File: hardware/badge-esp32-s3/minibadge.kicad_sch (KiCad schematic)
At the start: 10 parts, among them J10 Conn_01x02_Socket, J3 Conn_01x02_Socket, J4 Conn_01x02_Socket, J5 Conn_01x02_Socket, J6 Conn_01x04_Socket, J7 Conn_01x02_Socket, J8 Conn_01x04_Socket, J9 Conn_01x02_Socket

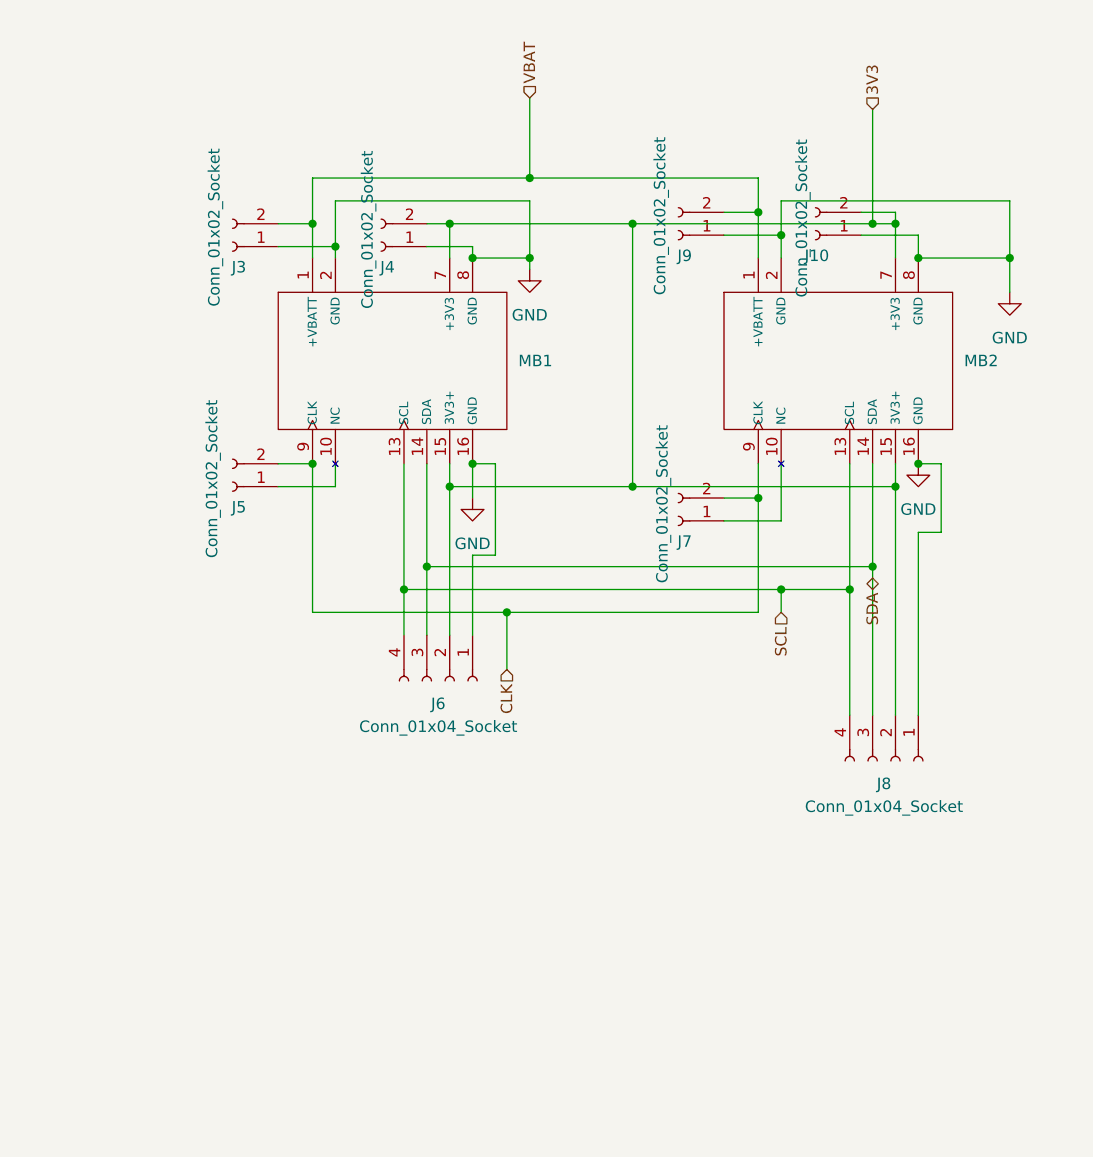
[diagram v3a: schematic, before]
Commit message: Added capacitors for the 5V booster circuit.
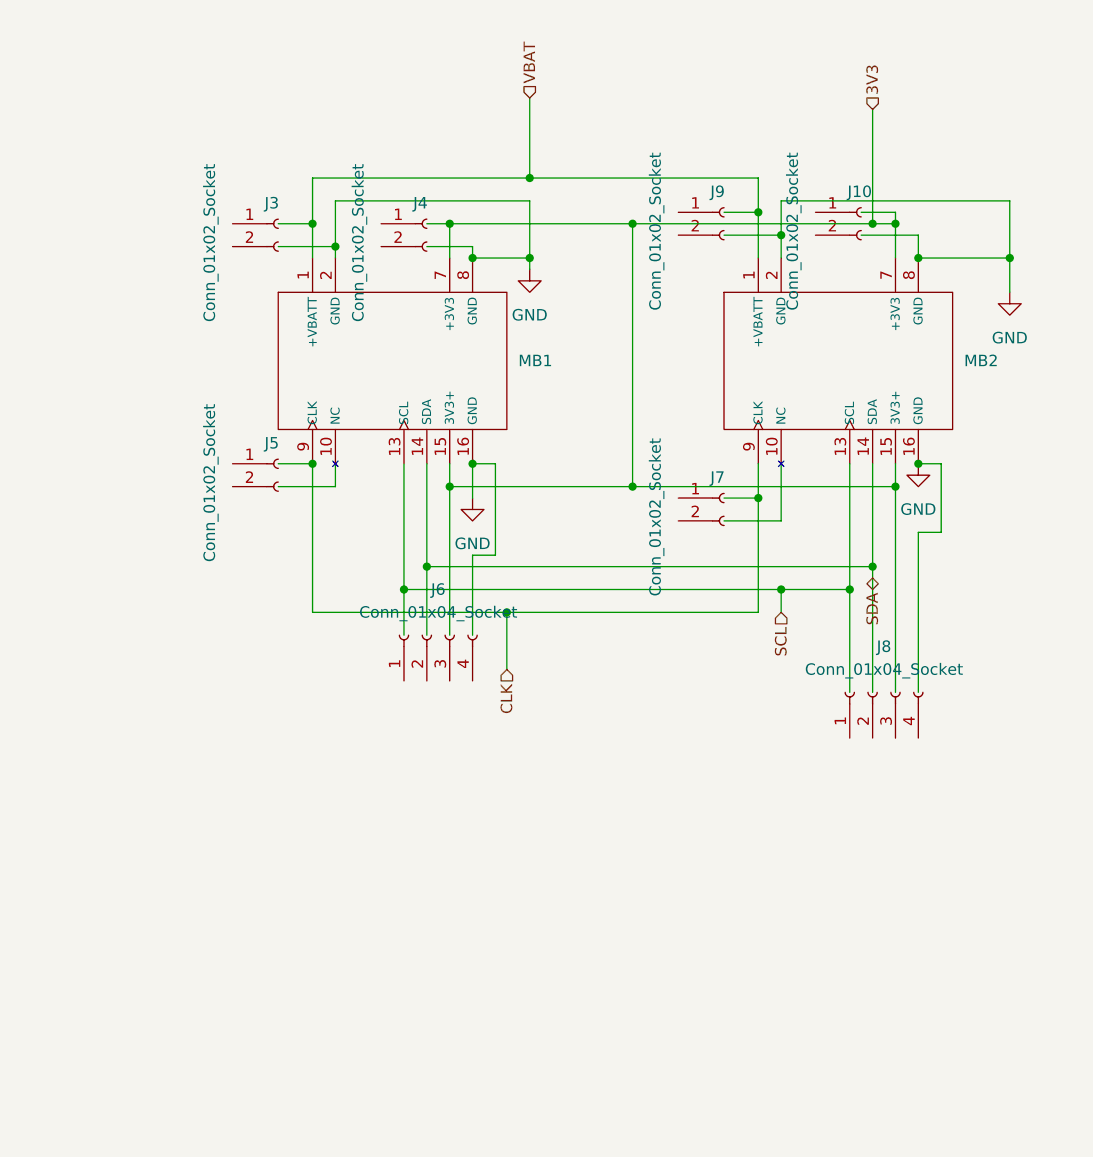
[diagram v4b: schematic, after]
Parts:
- J10, J3, J4, J5, J7, J9: footprint Connector_PinSocket_2.54mm:PinSocket_1x02_P2.54mm_Vertical -> Connector_PinHeader_2.54mm:PinHeader_1x02_P2.54mm_Vertical
- J6, J8: footprint Connector_PinSocket_2.54mm:PinSocket_1x04_P2.54mm_Vertical -> Connector_PinHeader_2.54mm:PinHeader_1x04_P2.54mm_Vertical
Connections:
- net 3V3: no longer J10.2 (Pin_2), J4.2 (Pin_2), J6.2 (Pin_2), J8.2 (Pin_2)
- net CLK: no longer J5.2 (Pin_2), J7.2 (Pin_2)
- net GND: no longer J10.1 (Pin_1), J3.1 (Pin_1), J4.1 (Pin_1), J6.1 (Pin_1), J8.1 (Pin_1), J9.1 (Pin_1)
- net SCL: no longer J6.4 (Pin_4), J8.4 (Pin_4)
- net SDA: no longer J6.3 (Pin_3), J8.3 (Pin_3)
- net VBAT: no longer J3.2 (Pin_2), J9.2 (Pin_2)
- net at J5.1 (Pin_1): no longer MB1.10 (NC)
- net at J7.1 (Pin_1): no longer MB2.10 (NC)
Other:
- moved on the sheet: J10, J3, J4, J5, J6, J7, J8, J9
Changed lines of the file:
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@@
-	(wire
-		(pts
-			(xy 154.94 100.33) (xy 154.94 114.3)
-		)
-		(stroke
-			(width 0)
-			(type default)
-		)
-	)
 	(wire
 		(pts
@@
 	(wire
 		(pts
-			(xy 157.48 97.79) (xy 157.48 114.3)
-		)
-		(stroke
-			(width 0)
-			(type default)
-		)
-	)
-	(wire
-		(pts
 			(xy 160.02 59.69) (xy 160.02 63.5)
 		)
@@
 	(wire
 		(pts
-			(xy 162.56 93.98) (xy 162.56 114.3)
-		)
-		(stroke
-			(width 0)
-			(type default)
-		)
-	)
-	(wire
-		(pts
 			(xy 113.03 105.41) (xy 113.03 96.52)
 		)
@@
 	(wire
 		(pts
+			(xy 154.94 100.33) (xy 154.94 111.76)
+		)
+		(stroke
+			(width 0)
+			(type default)
+		)
+	)
+	(wire
+		(pts
 			(xy 147.32 57.15) (xy 172.72 57.15)
 		)
@@
 	(wire
 		(pts
+			(xy 157.48 97.79) (xy 157.48 111.76)
+		)
+		(stroke
+			(width 0)
+			(type default)
+		)
+	)
+	(wire
+		(pts
 			(xy 165.1 93.98) (xy 165.1 86.36)
 		)
@@
 	(wire
 		(pts
-			(xy 160.02 88.9) (xy 160.02 114.3)
+			(xy 162.56 93.98) (xy 162.56 111.76)
 		)
 		(stroke
@@
 		(pts
 			(xy 105.41 100.33) (xy 147.32 100.33)
+		)
+		(stroke
+			(width 0)
+			(type default)
+		)
+	)
+	(wire
+		(pts
+			(xy 160.02 88.9) (xy 160.02 111.76)
 		)
 		(stroke
@@
 	(symbol
 		(lib_id "Connector:Conn_01x02_Socket")
-		(at 86.36 88.9 180)
+		(at 91.44 86.36 0)
 		(unit 1)
 		(exclude_from_sim no)
@@
 		(dnp no)
 		(property "Reference" "J5"
-			(at 87.884 91.186 0)
+			(at 89.916 84.074 0)
 			(effects
 				(font
@@
 		)
 		(property "Value" "Conn_01x02_Socket"
-			(at 84.074 79.248 90)
+			(at 83.82 97.282 90)
 			(effects
 				(font
@@
 			)
 		)
-		(property "Footprint" "Connector_PinSocket_2.54mm:PinSocket_1x02_P2.54mm_Vertical"
-			(at 86.36 88.9 0)
+		(property "Footprint" "Connector_PinHeader_2.54mm:PinHeader_1x02_P2.54mm_Vertical"
+			(at 91.44 86.36 0)
 			(effects
 				(font
@@
 		)
 		(property "Datasheet" "~"
-			(at 86.36 88.9 0)
+			(at 91.44 86.36 0)
 			(effects
 				(font
@@
 		)
 		(property "Description" "Generic connector, single row, 01x02, script generated"
-			(at 86.36 88.9 0)
+			(at 91.44 86.36 0)
 			(effects
 				(font
@@
 	(symbol
 		(lib_id "Connector:Conn_01x02_Socket")
-		(at 135.89 92.71 180)
+		(at 140.97 90.17 0)
 		(unit 1)
 		(exclude_from_sim no)
@@
 		(dnp no)
 		(property "Reference" "J7"
-			(at 137.414 94.996 0)
+			(at 139.446 87.884 0)
 			(effects
 				(font
@@
 		)
 		(property "Value" "Conn_01x02_Socket"
-			(at 134.112 82.042 90)
+			(at 133.35 101.092 90)
 			(effects
 				(font
@@
 			)
 		)
-		(property "Footprint" "Connector_PinSocket_2.54mm:PinSocket_1x02_P2.54mm_Vertical"
-			(at 135.89 92.71 0)
+		(property "Footprint" "Connector_PinHeader_2.54mm:PinHeader_1x02_P2.54mm_Vertical"
+			(at 140.97 90.17 0)
 			(effects
 				(font
@@
 		)
 		(property "Datasheet" "~"
-			(at 135.89 92.71 0)
+			(at 140.97 90.17 0)
 			(effects
 				(font
@@
 		)
 		(property "Description" "Generic connector, single row, 01x02, script generated"
-			(at 135.89 92.71 0)
+			(at 140.97 90.17 0)
 			(effects
 				(font
@@
 	(symbol
 		(lib_id "Connector:Conn_01x02_Socket")
-		(at 86.36 62.23 180)
+		(at 91.44 59.69 0)
 		(unit 1)
 		(exclude_from_sim no)
@@
 		(dnp no)
 		(property "Reference" "J3"
-			(at 87.884 64.516 0)
+			(at 89.916 57.404 0)
 			(effects
 				(font
@@
 		)
 		(property "Value" "Conn_01x02_Socket"
-			(at 84.328 51.308 90)
+			(at 83.82 70.612 90)
 			(effects
 				(font
@@
 			)
 		)
-		(property "Footprint" "Connector_PinSocket_2.54mm:PinSocket_1x02_P2.54mm_Vertical"
-			(at 86.36 62.23 0)
+		(property "Footprint" "Connector_PinHeader_2.54mm:PinHeader_1x02_P2.54mm_Vertical"
+			(at 91.44 59.69 0)
 			(effects
 				(font
@@
 		)
 		(property "Datasheet" "~"
-			(at 86.36 62.23 0)
+			(at 91.44 59.69 0)
 			(effects
 				(font
@@
 		)
 		(property "Description" "Generic connector, single row, 01x02, script generated"
-			(at 86.36 62.23 0)
+			(at 91.44 59.69 0)
 			(effects
 				(font
@@
 		)
 		(instances
-			(project "badge-esp32-s3"
+			(project ""
 				(path "/e2af9a6c-dbe9-4de2-9ba6-ea213a7300ec/18b0dd1f-1411-4aae-8334-5d13e6c2c6f9"
 					(reference "J3")
@@
 	(symbol
 		(lib_id "Connector:Conn_01x02_Socket")
-		(at 151.13 60.96 180)
+		(at 156.21 58.42 0)
 		(unit 1)
 		(exclude_from_sim no)
@@
 		(dnp no)
 		(property "Reference" "J10"
-			(at 152.654 63.246 0)
+			(at 154.686 56.134 0)
 			(effects
 				(font
@@
 		)
 		(property "Value" "Conn_01x02_Socket"
-			(at 149.606 50.292 90)
+			(at 148.59 69.342 90)
 			(effects
 				(font
@@
 			)
 		)
-		(property "Footprint" "Connector_PinSocket_2.54mm:PinSocket_1x02_P2.54mm_Vertical"
-			(at 151.13 60.96 0)
+		(property "Footprint" "Connector_PinHeader_2.54mm:PinHeader_1x02_P2.54mm_Vertical"
+			(at 156.21 58.42 0)
 			(effects
 				(font
@@
 		)
 		(property "Datasheet" "~"
-			(at 151.13 60.96 0)
+			(at 156.21 58.42 0)
 			(effects
 				(font
@@
 		)
 		(property "Description" "Generic connector, single row, 01x02, script generated"
-			(at 151.13 60.96 0)
+			(at 156.21 58.42 0)
 			(effects
 				(font
@@
 	(symbol
 		(lib_id "Connector:Conn_01x04_Socket")
-		(at 110.49 110.49 270)
+		(at 107.95 105.41 90)
 		(unit 1)
 		(exclude_from_sim no)
@@
 		(fields_autoplaced yes)
 		(property "Reference" "J6"
-			(at 109.22 113.03 90)
+			(at 109.22 100.33 90)
 			(effects
 				(font
@@
 		)
 		(property "Value" "Conn_01x04_Socket"
-			(at 109.22 115.57 90)
-			(effects
-				(font
-					(size 1.27 1.27)
-				)
-			)
-		)
-		(property "Footprint" "Connector_PinSocket_2.54mm:PinSocket_1x04_P2.54mm_Vertical"
-			(at 110.49 110.49 0)
+			(at 109.22 102.87 90)
+			(effects
+				(font
+					(size 1.27 1.27)
+				)
+			)
+		)
+		(property "Footprint" "Connector_PinHeader_2.54mm:PinHeader_1x04_P2.54mm_Vertical"
+			(at 107.95 105.41 0)
 			(effects
 				(font
@@
 		)
 		(property "Datasheet" "~"
-			(at 110.49 110.49 0)
+			(at 107.95 105.41 0)
 			(effects
 				(font
@@
 		)
 		(property "Description" "Generic connector, single row, 01x04, script generated"
-			(at 110.49 110.49 0)
+			(at 107.95 105.41 0)
 			(effects
 				(font
@@
 		)
 		(instances
-			(project "badge-esp32-s3"
+			(project ""
 				(path "/e2af9a6c-dbe9-4de2-9ba6-ea213a7300ec/18b0dd1f-1411-4aae-8334-5d13e6c2c6f9"
 					(reference "J6")
@@
 	(symbol
 		(lib_id "Connector:Conn_01x02_Socket")
-		(at 102.87 62.23 180)
+		(at 107.95 59.69 0)
 		(unit 1)
 		(exclude_from_sim no)
@@
 		(dnp no)
 		(property "Reference" "J4"
-			(at 104.394 64.516 0)
+			(at 106.426 57.404 0)
 			(effects
 				(font
@@
 		)
 		(property "Value" "Conn_01x02_Socket"
-			(at 101.346 51.562 90)
+			(at 100.33 70.612 90)
 			(effects
 				(font
@@
 			)
 		)
-		(property "Footprint" "Connector_PinSocket_2.54mm:PinSocket_1x02_P2.54mm_Vertical"
-			(at 102.87 62.23 0)
+		(property "Footprint" "Connector_PinHeader_2.54mm:PinHeader_1x02_P2.54mm_Vertical"
+			(at 107.95 59.69 0)
 			(effects
 				(font
@@
 		)
 		(property "Datasheet" "~"
-			(at 102.87 62.23 0)
+			(at 107.95 59.69 0)
 			(effects
 				(font
@@
 		)
 		(property "Description" "Generic connector, single row, 01x02, script generated"
-			(at 102.87 62.23 0)
+			(at 107.95 59.69 0)
 			(effects
 				(font
@@
 	(symbol
 		(lib_id "Connector:Conn_01x02_Socket")
-		(at 135.89 60.96 180)
+		(at 140.97 58.42 0)
 		(unit 1)
 		(exclude_from_sim no)
@@
 		(dnp no)
 		(property "Reference" "J9"
-			(at 137.414 63.246 0)
+			(at 139.446 56.134 0)
 			(effects
 				(font
@@
 		)
 		(property "Value" "Conn_01x02_Socket"
-			(at 133.858 50.038 90)
+			(at 133.35 69.342 90)
 			(effects
 				(font
@@
 			)
 		)
-		(property "Footprint" "Connector_PinSocket_2.54mm:PinSocket_1x02_P2.54mm_Vertical"
-			(at 135.89 60.96 0)
+		(property "Footprint" "Connector_PinHeader_2.54mm:PinHeader_1x02_P2.54mm_Vertical"
+			(at 140.97 58.42 0)
 			(effects
 				(font
@@
 		)
 		(property "Datasheet" "~"
-			(at 135.89 60.96 0)
+			(at 140.97 58.42 0)
 			(effects
 				(font
@@
 		)
 		(property "Description" "Generic connector, single row, 01x02, script generated"
-			(at 135.89 60.96 0)
+			(at 140.97 58.42 0)
 			(effects
 				(font
@@
 	(symbol
 		(lib_id "Connector:Conn_01x04_Socket")
-		(at 160.02 119.38 270)
+		(at 157.48 111.76 90)
 		(unit 1)
 		(exclude_from_sim no)
@@
 		(fields_autoplaced yes)
 		(property "Reference" "J8"
-			(at 158.75 121.92 90)
+			(at 158.75 106.68 90)
 			(effects
 				(font
@@
 		)
 		(property "Value" "Conn_01x04_Socket"
-			(at 158.75 124.46 90)
-			(effects
-				(font
-					(size 1.27 1.27)
-				)
-			)
-		)
-		(property "Footprint" "Connector_PinSocket_2.54mm:PinSocket_1x04_P2.54mm_Vertical"
-			(at 160.02 119.38 0)
+			(at 158.75 109.22 90)
+			(effects
+				(font
+					(size 1.27 1.27)
+				)
+			)
+		)
+		(property "Footprint" "Connector_PinHeader_2.54mm:PinHeader_1x04_P2.54mm_Vertical"
+			(at 157.48 111.76 0)
 			(effects
 				(font
@@
 		)
 		(property "Datasheet" "~"
-			(at 160.02 119.38 0)
+			(at 157.48 111.76 0)
 			(effects
 				(font
@@
 		)
 		(property "Description" "Generic connector, single row, 01x04, script generated"
-			(at 160.02 119.38 0)
-			(effects
-				(font
+			(at 157.48 111.76 0)
+			(effects
+				(font

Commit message: changed joystick and fixed minibadge in the schematic
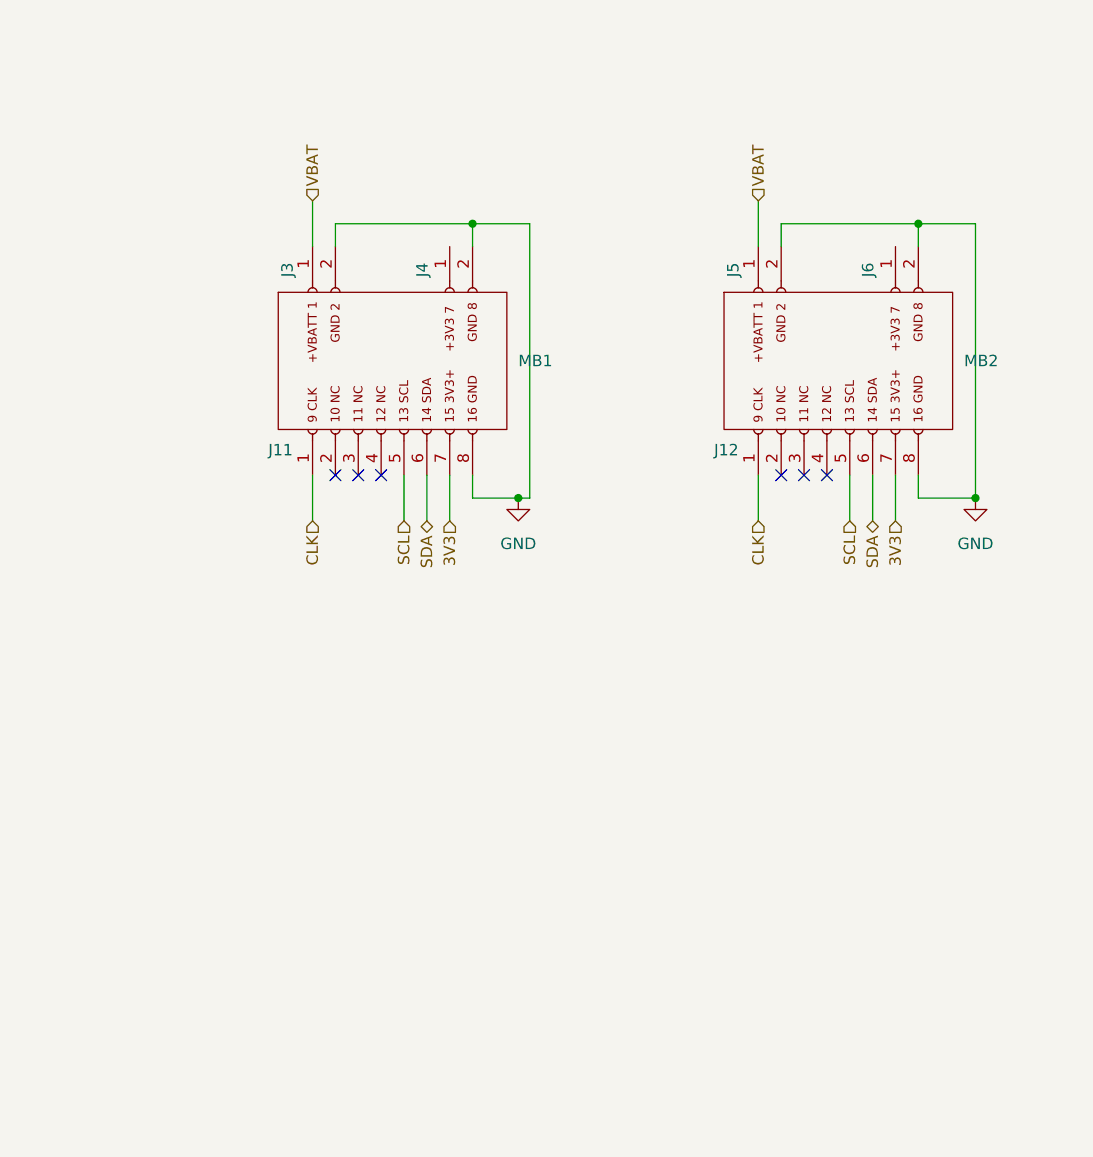
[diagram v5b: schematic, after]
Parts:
- removed J10, J7, J9: Conn_01x02_Socket, Connector_PinHeader_2.54mm:PinHeader_1x02_P2.54mm_Vertical, symbol Connector:Conn_01x02_Socket
- removed J6, J8: Conn_01x04_Socket, Connector_PinHeader_2.54mm:PinHeader_1x04_P2.54mm_Vertical, symbol Connector:Conn_01x04_Socket
- added J11, J12: Conn_01x08_Socket, symbol Connector:Conn_01x08_Socket
- added J6: Conn_01x02_Socket, Connector_PinHeader_2.54mm:PinHeader_1x02_P2.54mm_Vertical, symbol Connector:Conn_01x02_Socket
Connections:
- net 3V3: now also J11.7 (Pin_7), J12.7 (Pin_7); no longer MB1.15 (3V3+), MB1.7 (+3V3), MB2.15 (3V3+), MB2.7 (+3V3)
- net CLK: now also J11.1 (Pin_1), J12.1 (Pin_1); no longer MB1.9 (CLK), MB2.9 (CLK)
- net GND: now also J3.2 (Pin_2), J4.2 (Pin_2), J5.2 (Pin_2), J11.8 (Pin_8), J12.8 (Pin_8), J6.2 (Pin_2); no longer MB1.16 (GND), MB1.2 (GND), MB1.8 (GND), MB2.16 (GND), MB2.2 (GND), MB2.8 (GND)
- net SCL: now also J11.5 (Pin_5), J12.5 (Pin_5); no longer MB1.13 (SCL), MB2.13 (SCL)
- net SDA: now also J11.6 (Pin_6), J12.6 (Pin_6); no longer MB1.14 (SDA), MB2.14 (SDA)
- net VBAT: now also J3.1 (Pin_1), J5.1 (Pin_1); no longer MB1.1 (+VBATT), MB2.1 (+VBATT)
- no-connect marks 0 -> 6
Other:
- moved on the sheet: J3

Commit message: almost finished
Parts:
- removed J11, J12: Conn_01x08_Socket, symbol Connector:Conn_01x08_Socket
- removed J3, J4, J6: Conn_01x02_Socket, Connector_PinHeader_2.54mm:PinHeader_1x02_P2.54mm_Vertical, symbol Connector:Conn_01x02_Socket
- added J12: Conn_01x02_Socket, Connector_PinHeader_2.54mm:PinHeader_1x02_P2.54mm_Vertical, symbol Connector:Conn_01x02_Socket
- added J13, J6: Conn_01x04_Socket, Connector_PinHeader_2.54mm:PinHeader_1x04_P2.54mm_Vertical, symbol Connector:Conn_01x04_Socket
- added J7, J8: Conn_01x08_Socket, Connector_PinHeader_2.54mm:PinHeader_1x08_P2.54mm_Vertical, symbol Connector:Conn_01x08_Socket
- added J9: Conn_02x06_Odd_Even, Connector_PinHeader_2.54mm:PinHeader_2x06_P2.54mm_Vertical, symbol Connector_Generic:Conn_02x06_Odd_Even
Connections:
- net 3V3: now also J13.3 (Pin_3), J6.3 (Pin_3), J7.7 (Pin_7), J8.7 (Pin_7)
- net GND: now also J13.4 (Pin_4), J6.4 (Pin_4), J7.2 (Pin_2), J7.8 (Pin_8), J8.2 (Pin_2), J8.8 (Pin_8); no longer J5.2 (Pin_2)
- net SCL: now also J13.1 (Pin_1), J6.1 (Pin_1)
- net SDA: now also J13.2 (Pin_2), J6.2 (Pin_2)
- net VBAT: now also J7.1 (Pin_1), J8.1 (Pin_1); no longer J5.1 (Pin_1)
- new net B1CLK: J9.2 (Pin_2)
- new net B1IO1: J9.6 (Pin_6)
- new net B1IO2: J9.4 (Pin_4)
- new net B2CLK: J9.8 (Pin_8)
- new net B2IO1: J9.12 (Pin_12)
- new net B2IO2: J9.10 (Pin_10)
- new net MB1CLK: J5.1 (Pin_1), J9.1 (Pin_1)
- new net MB1IO1: J7.3 (Pin_3), J9.5 (Pin_5)
- new net MB1IO2: J7.4 (Pin_4), J9.3 (Pin_3)
- new net MB2CLK: J12.1 (Pin_1), J9.7 (Pin_7)
- new net MB2IO1: J8.3 (Pin_3), J9.11 (Pin_11)
- new net MB2IO2: J8.4 (Pin_4), J9.9 (Pin_9)

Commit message: final changes and part updated
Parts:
- added R40, R47, R49, R50, R51, R52: 100Ω, PCM_JLCPCB:R_0402, symbol PCM_JLCPCB-Resistors:0402,100Ω
- J12, J5: footprint Connector_PinHeader_2.54mm:PinHeader_1x02_P2.54mm_Vertical -> Connector_PinSocket_2.54mm:PinSocket_1x02_P2.54mm_Vertical; LCSC (none) -> C7499322
- J13, J6: footprint Connector_PinHeader_2.54mm:PinHeader_1x04_P2.54mm_Vertical -> Connector_PinSocket_2.54mm:PinSocket_1x04_P2.54mm_Vertical; LCSC (none) -> C2718488
- J7, J8: footprint Connector_PinHeader_2.54mm:PinHeader_1x08_P2.54mm_Vertical -> Connector_PinSocket_2.54mm:PinSocket_1x08_P2.54mm_Vertical; LCSC (none) -> C42431862
- J9: footprint Connector_PinHeader_2.54mm:PinHeader_2x06_P2.54mm_Vertical -> Connector_PinSocket_2.54mm:PinSocket_2x06_P2.54mm_Vertical; LCSC (none) -> C5307342
- MB1, MB2: now left out of the parts list
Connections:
- net B1CLK: now also J9.1 (Pin_1); no longer J9.2 (Pin_2)
- net B1IO1: now also J9.5 (Pin_5); no longer J9.6 (Pin_6)
- net B1IO2: now also J9.3 (Pin_3); no longer J9.4 (Pin_4)
- net B2CLK: now also J9.7 (Pin_7); no longer J9.8 (Pin_8)
- net B2IO1: now also J9.11 (Pin_11); no longer J9.12 (Pin_12)
- net B2IO2: now also J9.9 (Pin_9); no longer J9.10 (Pin_10)
- net MB1CLK: now also J9.2 (Pin_2), R49.2; no longer J5.1 (Pin_1), J9.1 (Pin_1)
- net MB1IO1: now also J9.6 (Pin_6), R40.1; no longer J7.3 (Pin_3), J9.5 (Pin_5)
- net MB1IO2: now also J9.4 (Pin_4), R47.1; no longer J7.4 (Pin_4), J9.3 (Pin_3)
- net MB2CLK: now also J9.8 (Pin_8), R52.2; no longer J12.1 (Pin_1), J9.7 (Pin_7)
- net MB2IO1: now also J9.12 (Pin_12), R50.1; no longer J8.3 (Pin_3), J9.11 (Pin_11)
- net MB2IO2: now also J9.10 (Pin_10), R51.1; no longer J8.4 (Pin_4), J9.9 (Pin_9)
- new net: J8.4 (Pin_4), R51.2
- new net: J7.3 (Pin_3), R40.2
- new net: J7.4 (Pin_4), R47.2
- new net: J12.1 (Pin_1), R52.1
- new net: J8.3 (Pin_3), R50.2
- new net: J5.1 (Pin_1), R49.1
